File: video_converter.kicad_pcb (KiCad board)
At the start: 4 copper layers, 55 x 64 mm, 76 parts, among them J1 S4B-ZR-SM4A-TF(LF)(SN), J2 Conn_01x09_Male, J3 Conn_02x06_Odd_Even, J4 Conn_02x06_Odd_Even, J5 Conn_02x06_Odd_Even, J6 2-1734592-4, J7 Screw_Terminal_01x02, SW1 SW_DIP_x02, U1 ADV7180BSTZ, U2 AMS1117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

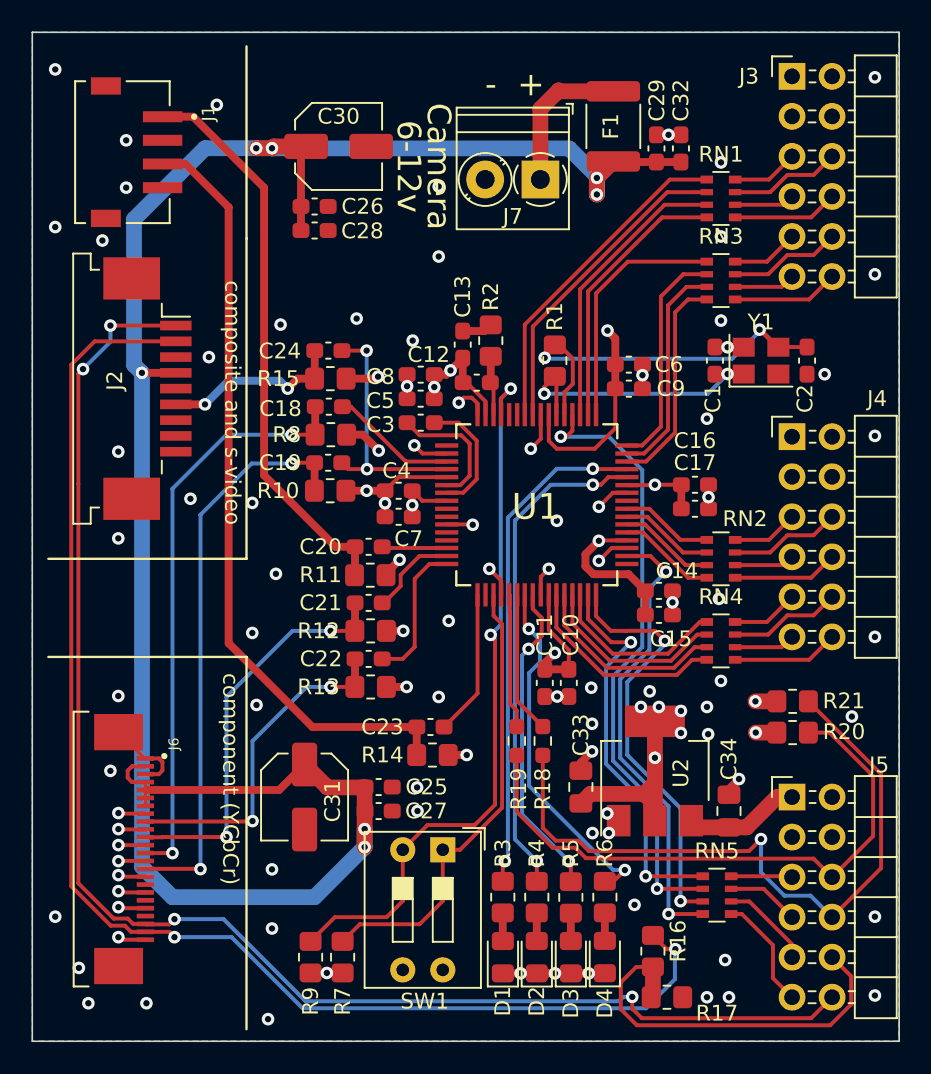
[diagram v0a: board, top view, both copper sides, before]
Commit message: updated layout
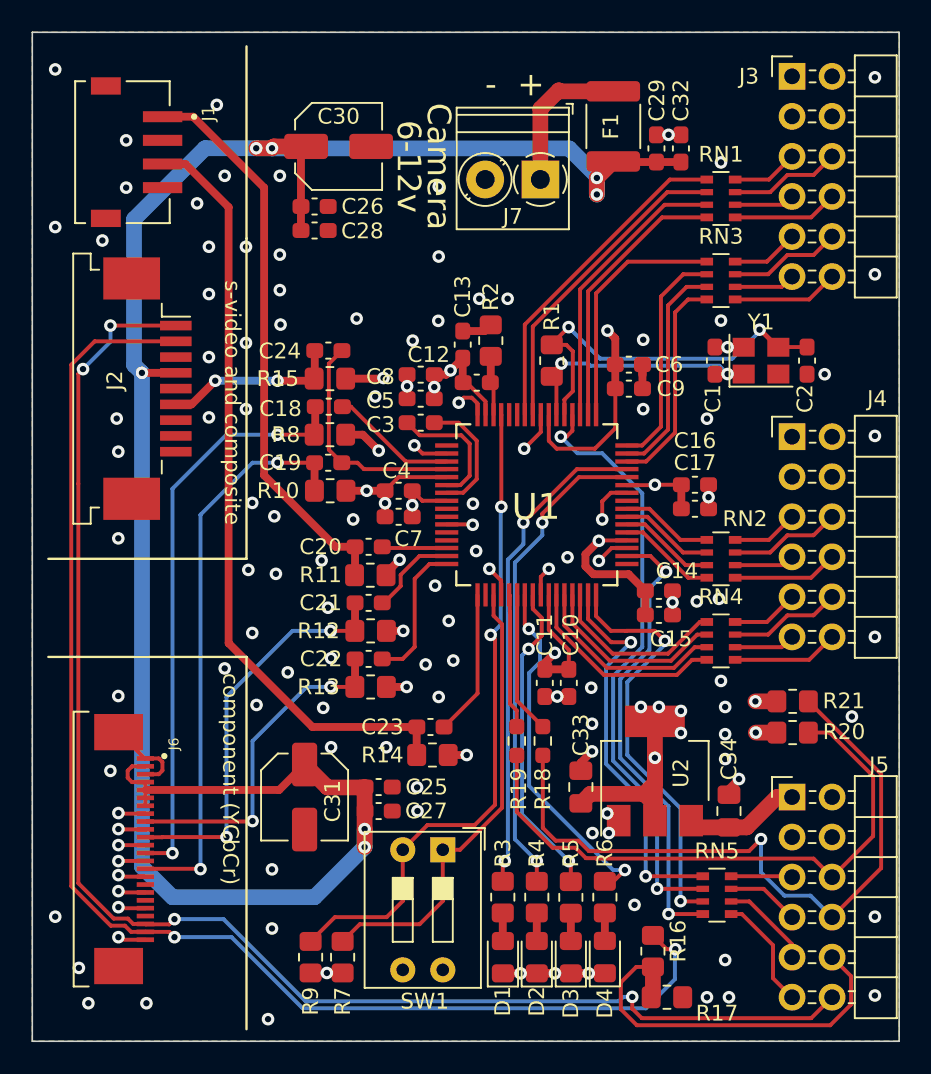
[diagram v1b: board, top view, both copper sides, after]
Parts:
- moved R1 0.19 mm to (147.0, 77.7)
- moved R8 0.06 mm to (132.9, 82.4)
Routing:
- net Net-(R9-Pad1): track 46.1 -> 42.3 mm
- net XTAL: track 17.8 -> 16.3 mm
- net Net-(C19-Pad2): track 15.9 -> 14.6 mm, vias 2 -> 0
- net GND: track 78.8 -> 80.1 mm, vias 96 -> 128
- net Net-(RN5-Pad2): track 39.3 -> 38.5 mm
- net Net-(R3-Pad1): track 32.1 -> 31.3 mm
- net Net-(R4-Pad1): track 31.7 -> 30.9 mm
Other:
- board text added: "s-video and composite"
- board text removed: "composite and s-video"

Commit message: fixed bad routing
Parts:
- added R22: 0R, Resistor_SMD:R_0603_1608Metric, F.Cu at (136.0, 77.1)
- R4: value R -> 330R
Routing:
- net Net-(C18-Pad2): track 8.06 -> 13.1 mm
- net GND: track 80.1 -> 78.6 mm, vias 128 -> 129
- net Net-(C19-Pad2): track 14.6 -> 16.1 mm
- net Net-(R3-Pad1): track 31.3 -> 32.0 mm
